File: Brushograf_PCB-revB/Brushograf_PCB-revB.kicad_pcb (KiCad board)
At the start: 2 copper layers, 170 x 85 mm, 72 parts, among them J1 Conn_01x05_Socket, J12 USB-C PD in, J13 Pendant, J2 Conn_01x05_Socket, J3 Conn_01x05_Socket, J8 SD_CARD_MICRO_AMPHENOL_114008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, SW1 ESP POWER, SW2 SW_Lever_1P2T_NKK_GW12LxH, U1 ULN2003A, U2 ULN2003A, U3 ULN2003A, U4 ESP32-DevKitC, U6 CH224K, U7 TPS54202, U8 TPS54202

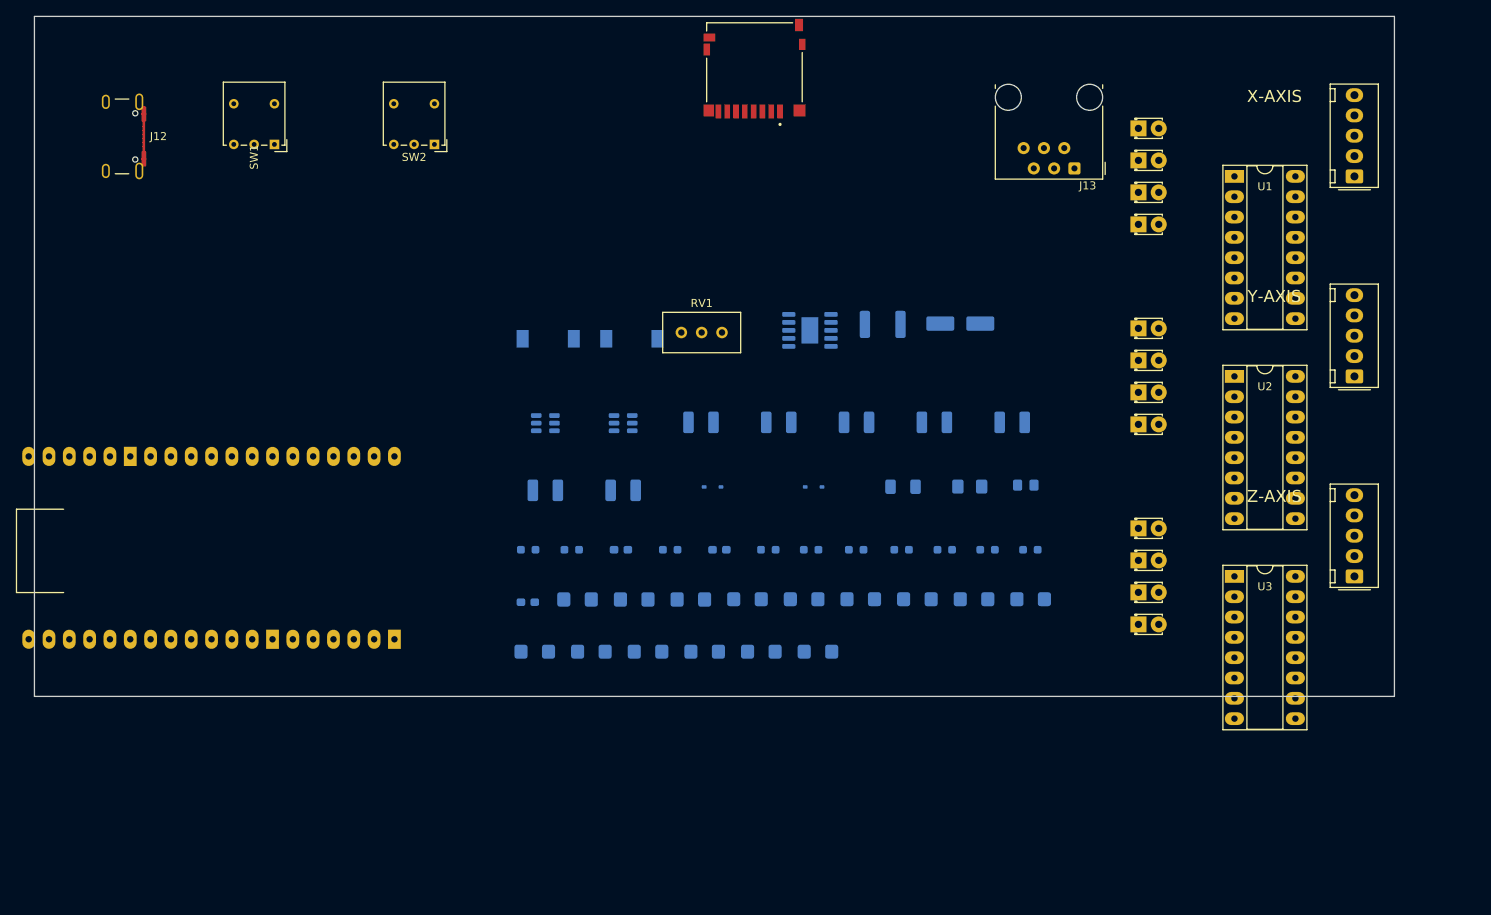
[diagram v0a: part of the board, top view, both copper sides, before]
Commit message: Motor connectors/drivers to bottom edge (Z, X, Y), preserve length
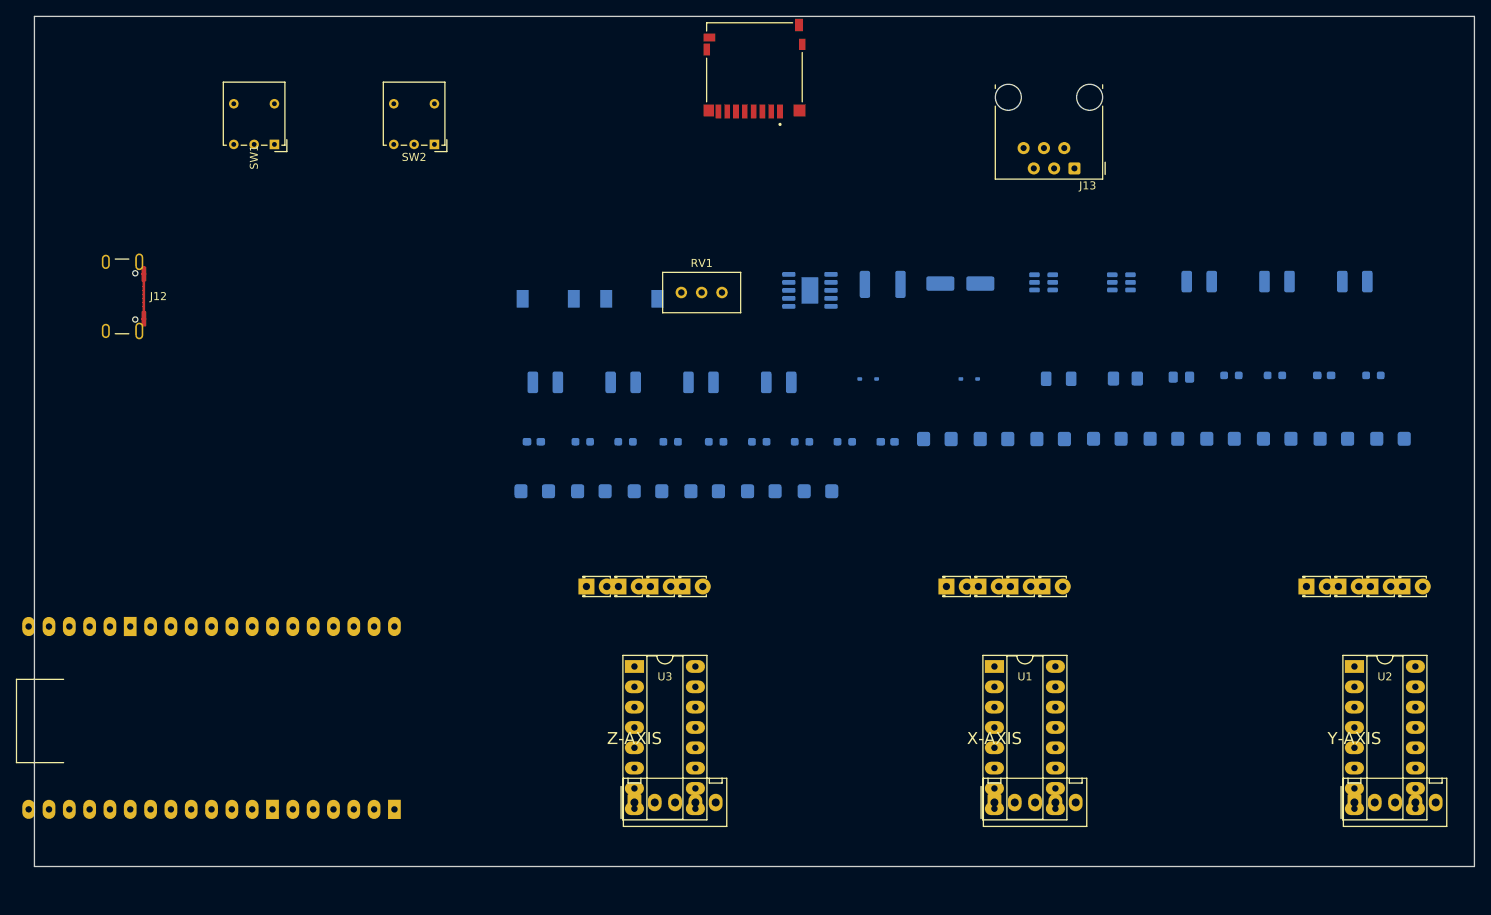
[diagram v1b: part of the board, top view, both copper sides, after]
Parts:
- moved J3 94.3 mm to (85.0, 108.3), turned to 0 degrees
- moved R27 90.6 mm to (159.6, 54.9)
- moved C16 90.6 mm to (171.2, 54.9)
- moved R24 90.6 mm to (165.1, 54.9)
- moved R22 90.6 mm to (177.4, 54.9)
- moved J1 90.3 mm to (130.0, 108.3), turned to 0 degrees
- moved U3 75.8 mm to (85.0, 91.3)
- moved D9 69.4 mm to (79.0, 81.3)
- moved U1 68.2 mm to (130.0, 91.3)
- moved D10 65.1 mm to (83.0, 81.3)
- moved U7 64.7 mm to (136.1, 43.2)
- moved U8 64.7 mm to (145.9, 43.2)
- moved C10 64.7 mm to (165.3, 43.1)
- moved C11 64.7 mm to (155.6, 43.1)
- moved C8 64.7 mm to (175.0, 43.1)
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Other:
- board size 170 x 85 mm -> 180 x 106.3 mm

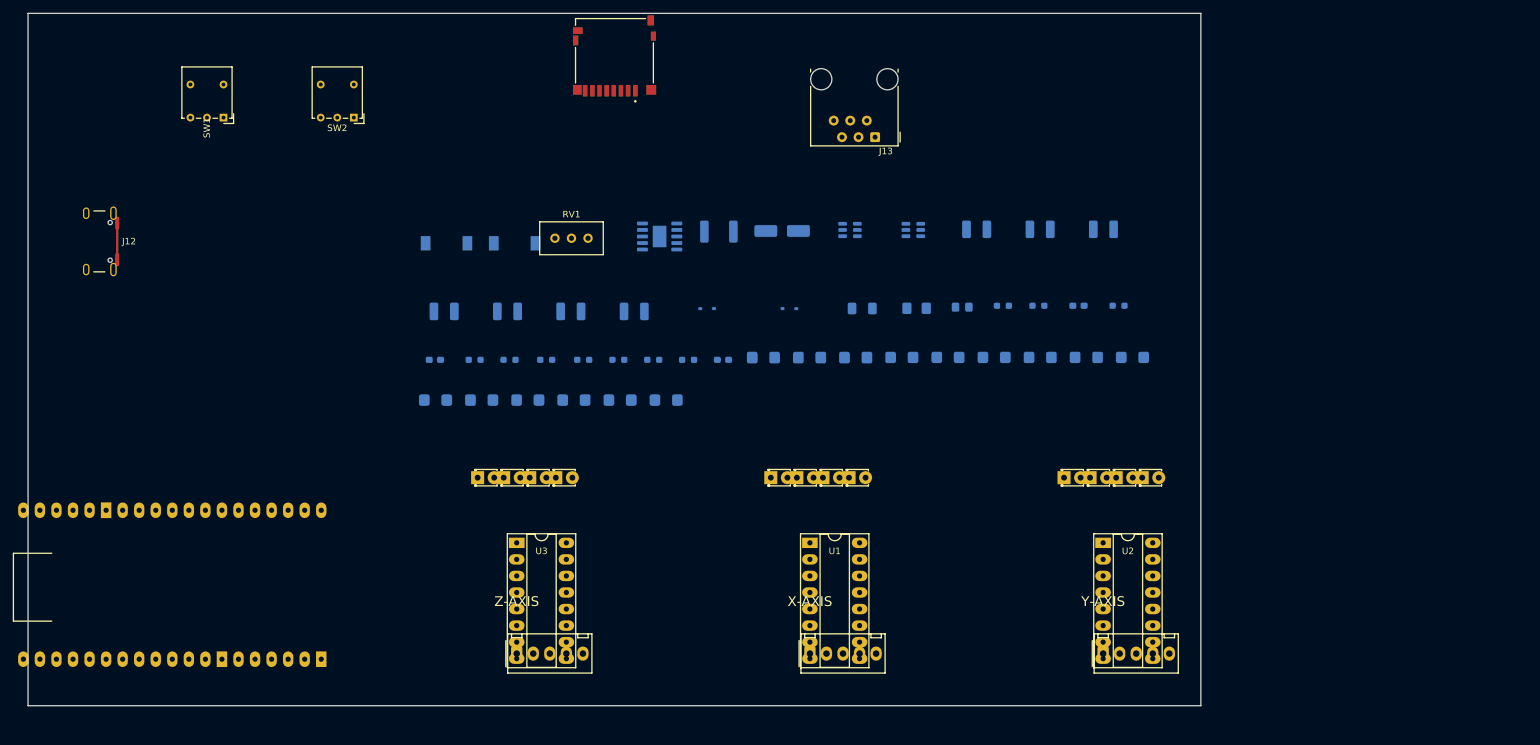
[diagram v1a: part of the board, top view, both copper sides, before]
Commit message: Make board much wider (230mm) and unstack sockets/connectors
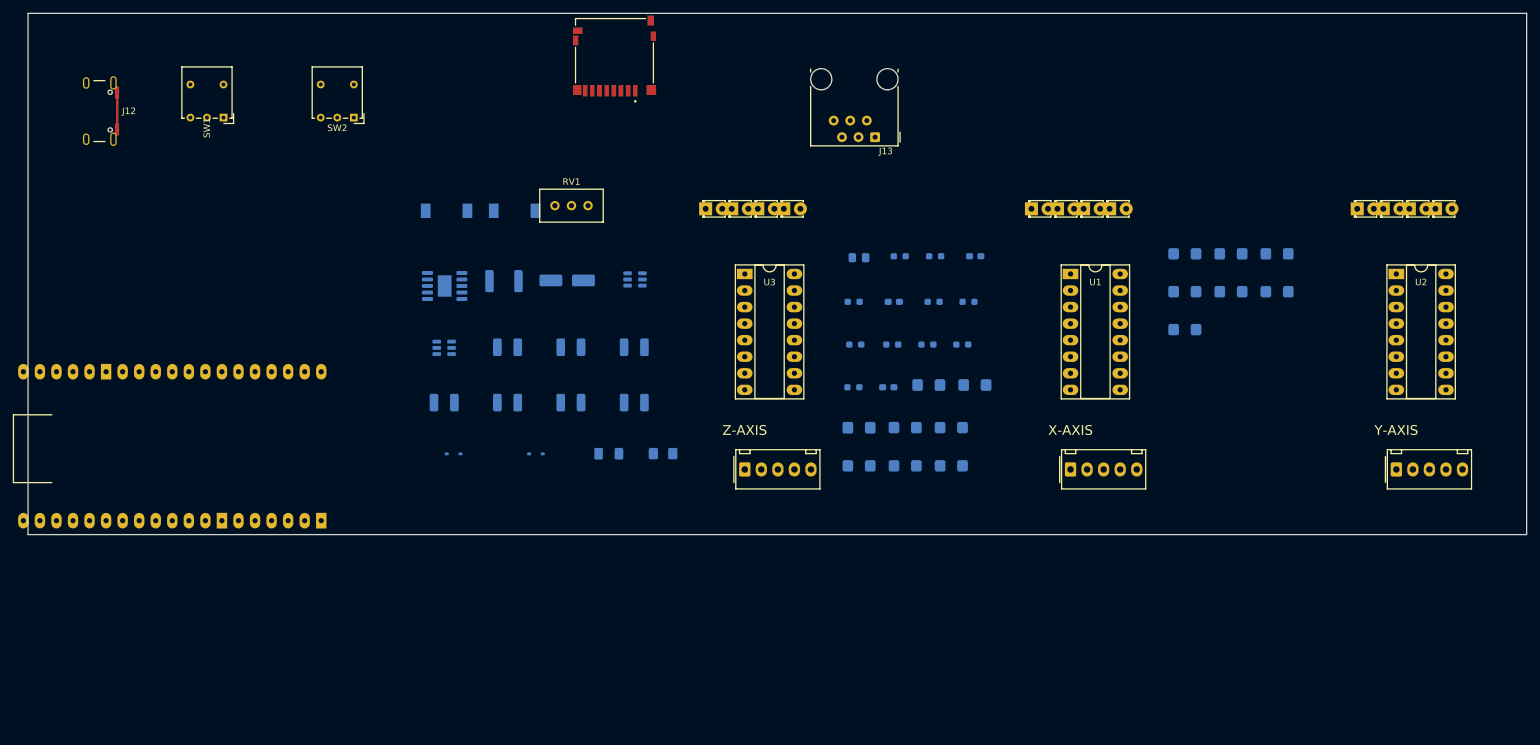
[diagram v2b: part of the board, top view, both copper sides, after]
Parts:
- moved R7 124.1 mm to (194.6, 46.9)
- moved R10 124.1 mm to (201.7, 46.9)
- moved R5 102.2 mm to (194.6, 52.7)
- moved R3 102.2 mm to (201.7, 52.7)
- moved R8 102.2 mm to (187.5, 52.7)
- moved R1 80.3 mm to (187.5, 58.5)
- moved C10 74.2 mm to (93.3, 61.2)
- moved C11 74.2 mm to (83.6, 61.2)
- moved C8 74.2 mm to (103.0, 61.2)
- moved U8 74.2 mm to (73.9, 61.3)
- moved C12 71.0 mm to (142.9, 54.3)
- moved R28 71.0 mm to (149.0, 54.3)
- moved R31 71.0 mm to (154.3, 54.3)
- moved D5 61.1 mm to (214.0, 40.0)
- moved D6 61.1 mm to (218.0, 40.0)
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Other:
- board size 180 x 106.3 mm -> 230 x 80 mm

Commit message: Move motor LEDs below connectors, flush mount USB-C edge
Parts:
- moved D1 46.0 mm to (164.0, 86.0)
- moved D10 46.0 mm to (118.0, 86.0)
- moved D11 46.0 mm to (122.0, 86.0)
- moved D12 46.0 mm to (126.0, 86.0)
- moved D2 46.0 mm to (168.0, 86.0)
- moved D3 46.0 mm to (172.0, 86.0)
- moved D4 46.0 mm to (176.0, 86.0)
- moved D5 46.0 mm to (214.0, 86.0)
- moved D6 46.0 mm to (218.0, 86.0)
- moved D7 46.0 mm to (222.0, 86.0)
- moved D8 46.0 mm to (226.0, 86.0)
- moved D9 46.0 mm to (114.0, 86.0)
- moved J1 5.00 mm to (170.0, 75.0)
- moved J2 5.00 mm to (220.0, 75.0)
- moved J3 5.00 mm to (120.0, 75.0)
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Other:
- board size 230 x 80 mm -> 230 x 85 mm
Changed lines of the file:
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@@
 	(footprint "009_Brushograph:LED_D1.8mm_Brushograf"
 		(layer "F.Cu")
-		(at 168 40)
+		(at 168 86)
 		(descr "LED, Round, Rectangular, size 3.3x2.4mm, diameter 1.8mm, 2 pins, generated by kicad-footprint-generator")
 		(tags "LED")
@@
 	(footprint "009_Brushograph:LED_D1.8mm_Brushograf"
 		(layer "F.Cu")
-		(at 122 40)
+		(at 122 86)
 		(descr "LED, Round, Rectangular, size 3.3x2.4mm, diameter 1.8mm, 2 pins, generated by kicad-footprint-generator")
 		(tags "LED")
@@
 	(footprint "009_Brushograph:Molex_1x05_P2.54mm_Brushograf"
 		(layer "F.Cu")
-		(at 120 80)
+		(at 120 75)
 		(descr "Molex KK-254 Interconnect System, old/engineering part number: AE-6410-05A example for new part number: 22-27-2051, 5 Pins (http://www.molex.com/pdm_docs/sd/022272021_sd.pdf), generated with kicad-footprint-generator")
 		(tags "connector Molex KK-254 vertical")
@@
 	(footprint "009_Brushograph:LED_D1.8mm_Brushograf"
 		(layer "F.Cu")
-		(at 114 40)
+		(at 114 86)
 		(descr "LED, Round, Rectangular, size 3.3x2.4mm, diameter 1.8mm, 2 pins, generated by kicad-footprint-generator")
 		(tags "LED")
@@
 	(footprint "009_Brushograph:LED_D1.8mm_Brushograf"
 		(layer "F.Cu")
-		(at 222 40)
+		(at 222 86)
 		(descr "LED, Round, Rectangular, size 3.3x2.4mm, diameter 1.8mm, 2 pins, generated by kicad-footprint-generator")
 		(tags "LED")
@@
 	(footprint "009_Brushograph:LED_D1.8mm_Brushograf"
 		(layer "F.Cu")
-		(at 126 40)
+		(at 126 86)
 		(descr "LED, Round, Rectangular, size 3.3x2.4mm, diameter 1.8mm, 2 pins, generated by kicad-footprint-generator")
 		(tags "LED")
@@
 	(footprint "009_Brushograph:LED_D1.8mm_Brushograf"
 		(layer "F.Cu")
-		(at 118 40)
+		(at 118 86)
 		(descr "LED, Round, Rectangular, size 3.3x2.4mm, diameter 1.8mm, 2 pins, generated by kicad-footprint-generator")
 		(tags "LED")
@@
 	(footprint "009_Brushograph:LED_D1.8mm_Brushograf"
 		(layer "F.Cu")
-		(at 218 40)
+		(at 218 86)
 		(descr "LED, Round, Rectangular, size 3.3x2.4mm, diameter 1.8mm, 2 pins, generated by kicad-footprint-generator")
 		(tags "LED")
@@
 	(footprint "Connector_USB:USB_C_Receptacle_GCT_USB4105-xx-A_16P_TopMnt_Horizontal"
 		(layer "F.Cu")
-		(at 20 25 -90)
+		(at 20.196 25 -90)
 		(descr "USB 2.0 Type C Receptacle, GCT, 16P, top mounted, horizontal, 5A: https://gct.co/files/drawings/usb4105.pdf")
 		(tags "USB C Type-C Receptacle SMD USB 2.0 16P 16C USB4105-15-A USB4105-15-A-060 USB4105-15-A-120 USB4105-GF-A USB4105-GF-A-060 USB4105-GF-A-120")
@@
 	(footprint "009_Brushograph:LED_D1.8mm_Brushograf"
 		(layer "F.Cu")
-		(at 172 40)
+		(at 172 86)
 		(descr "LED, Round, Rectangular, size 3.3x2.4mm, diameter 1.8mm, 2 pins, generated by kicad-footprint-generator")
 		(tags "LED")
@@
 	(footprint "009_Brushograph:LED_D1.8mm_Brushograf"
 		(layer "F.Cu")
-		(at 214 40)
+		(at 214 86)
 		(descr "LED, Round, Rectangular, size 3.3x2.4mm, diameter 1.8mm, 2 pins, generated by kicad-footprint-generator")
 		(tags "LED")
@@
 	(footprint "009_Brushograph:Molex_1x05_P2.54mm_Brushograf"
 		(layer "F.Cu")
-		(at 220 80)
+		(at 220 75)
 		(descr "Molex KK-254 Interconnect System, old/engineering part number: AE-6410-05A example for new part number: 22-27-2051, 5 Pins (http://www.molex.com/pdm_docs/sd/022272021_sd.pdf), generated with kicad-footprint-generator")
 		(tags "connector Molex KK-254 vertical")
@@
 	(footprint "009_Brushograph:LED_D1.8mm_Brushograf"
 		(layer "F.Cu")
-		(at 176 40)
+		(at 176 86)
 		(descr "LED, Round, Rectangular, size 3.3x2.4mm, diameter 1.8mm, 2 pins, generated by kicad-footprint-generator")
 		(tags "LED")
@@
 	(footprint "009_Brushograph:Molex_1x05_P2.54mm_Brushograf"
 		(layer "F.Cu")
-		(at 170 80)
+		(at 170 75)
 		(descr "Molex KK-254 Interconnect System, old/engineering part number: AE-6410-05A example for new part number: 22-27-2051, 5 Pins (http://www.molex.com/pdm_docs/sd/022272021_sd.pdf), generated with kicad-footprint-generator")
 		(tags "connector Molex KK-254 vertical")
@@
 	(footprint "009_Brushograph:LED_D1.8mm_Brushograf"
 		(layer "F.Cu")
-		(at 164 40)
+		(at 164 86)
 		(descr "LED, Round, Rectangular, size 3.3x2.4mm, diameter 1.8mm, 2 pins, generated by kicad-footprint-generator")
 		(tags "LED")
@@
 	(footprint "009_Brushograph:LED_D1.8mm_Brushograf"
 		(layer "F.Cu")
-		(at 226 40)
+		(at 226 86)
 		(descr "LED, Round, Rectangular, size 3.3x2.4mm, diameter 1.8mm, 2 pins, generated by kicad-footprint-generator")
 		(tags "LED")
@@
 	)
 	(gr_line
-		(start 10 90)
+		(start 10 95)
 		(end 10 10)
 		(stroke
@@
 	(gr_line
 		(start 240 10)
-		(end 240 90)
+		(end 240 95)
 		(stroke
 			(width 0.1)
@@
 	)
 	(gr_line
-		(start 240 90)
-		(end 10 90)
+		(start 240 95)
+		(end 10 95)
 		(stroke
 			(width 0.1)
@@
 	)
 	(gr_text "Z-AXIS"
-		(at 120 74 0)
+		(at 120 69 0)
 		(layer "F.SilkS")
 		(effects
@@
 	)
 	(gr_text "X-AXIS"
-		(at 170 74 0)
+		(at 170 69 0)
 		(layer "F.SilkS")
 		(effects
@@
 	)
 	(gr_text "Y-AXIS"
-		(at 220 74 0)
+		(at 220 69 0)
 		(layer "F.SilkS")
 		(effects
